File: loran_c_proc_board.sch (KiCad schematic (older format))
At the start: 28 parts, among them P101 Power, P102 Cortex SWD, P103 Clock board, U101 LD1117S33, U102 74AC14, U103 74AC14

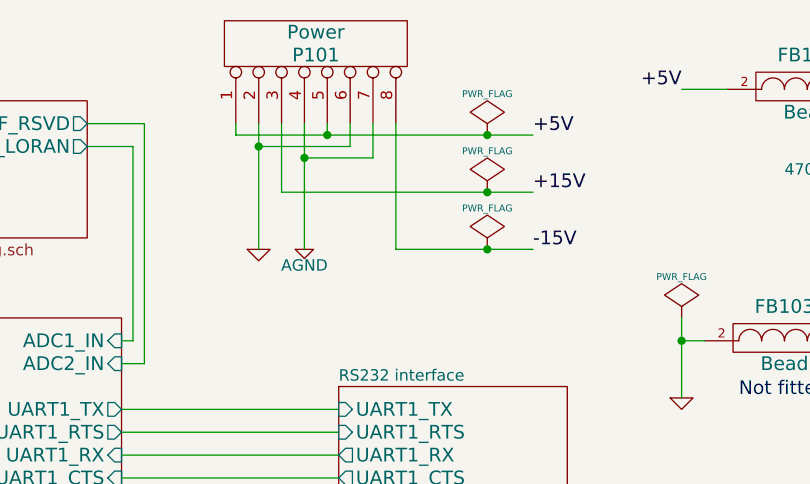
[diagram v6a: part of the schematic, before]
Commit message: Intermediate update: PCB routing/schematic tweaking in process..
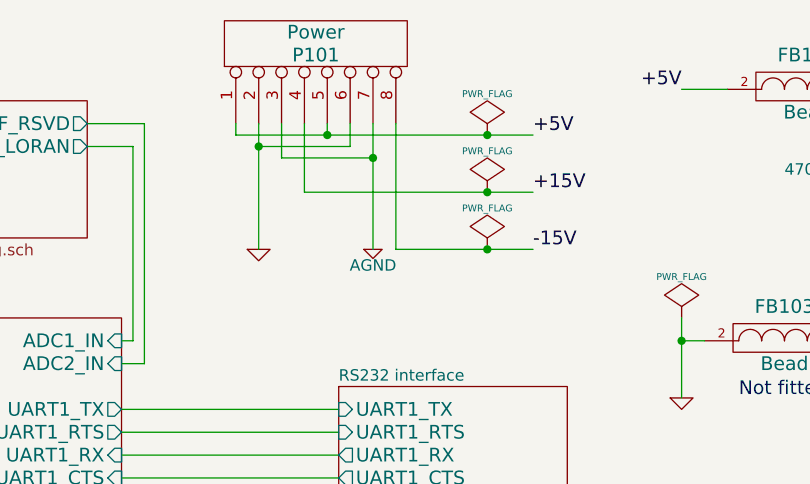
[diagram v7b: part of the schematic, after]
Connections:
- net +15V: now also P101.4 (P4); no longer P101.3 (P3)
- net AGND: now also P101.3 (P3); no longer P101.4 (P4)
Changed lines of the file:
@@
 L AGND #PWR012
 U 1 1 52E69A33
-P 5000 1850
-F 0 "#PWR012" H 5000 1850 40  0001 C CNN
-F 1 "AGND" H 5000 1780 50  0000 C CNN
-F 2 "" H 5000 1850 60  0000 C CNN
-F 3 "" H 5000 1850 60  0000 C CNN
-	1    5000 1850
+P 5300 1850
+F 0 "#PWR012" H 5300 1850 40  0001 C CNN
+F 1 "AGND" H 5300 1780 50  0000 C CNN
+F 2 "" H 5300 1850 60  0000 C CNN
+F 3 "" H 5300 1850 60  0000 C CNN
+	1    5300 1850
 	1    0    0    -1
 $EndComp
@@
 	5200 1400 5200 1300
 Wire Wire Line
-	5000 1300 5000 1850
-Wire Wire Line
-	5000 1450 5300 1450
-Wire Wire Line
-	5300 1450 5300 1300
+	4900 1450 5300 1450
+Wire Wire Line
+	5300 1300 5300 1850
 Connection ~ 5100 1350
 Wire Wire Line
-	4900 1300 4900 1600
-Wire Wire Line
-	4900 1600 6000 1600
+	5000 1600 6000 1600
 Wire Wire Line
 	5400 1300 5400 1850
@@
 Connection ~ 5800 1850
 Connection ~ 4800 1400
-Connection ~ 5000 1450
+Wire Wire Line
+	5000 1300 5000 1600
+Wire Wire Line
+	4900 1300 4900 1450
+Connection ~ 5300 1450
 $EndSCHEMATC

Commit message: Intermediate update #2: PCB routing/schematic tweaking in process
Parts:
- added MH101, MH102, MH103, MH104: HOLE, symbol HOLE
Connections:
- net GNDPWR: now also MH103.1, MH104.1
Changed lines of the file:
@@
 LIBS:transf
 LIBS:video
+LIBS:led_holder
 LIBS:loran_c_proc_board-cache
 EELAYER 24 0
@@
 	4900 1300 4900 1450
 Connection ~ 5300 1450
+$Comp
+L HOLE MH104
+U 1 1 52EF52BD
+P 1800 1800
+F 0 "MH104" H 1800 2000 60  0000 C CNN
+F 1 "HOLE" H 1800 1620 60  0000 C CNN
+F 2 "" H 1800 1800 60  0000 C CNN
+F 3 "" H 1800 1800 60  0000 C CNN
+	1    1800 1800
+	1    0    0    -1
+$EndComp
+$Comp
+L HOLE MH103
+U 1 1 52EF53B0
+P 1800 1250
+F 0 "MH103" H 1800 1450 60  0000 C CNN
+F 1 "HOLE" H 1800 1070 60  0000 C CNN
+F 2 "" H 1800 1250 60  0000 C CNN
+F 3 "" H 1800 1250 60  0000 C CNN
+	1    1800 1250
+	1    0    0    -1
+$EndComp
+$Comp
+L HOLE MH101
+U 1 1 52EF7090
+P 1000 1250
+F 0 "MH101" H 1000 1450 60  0000 C CNN
+F 1 "HOLE" H 1000 1070 60  0000 C CNN
+F 2 "" H 1000 1250 60  0000 C CNN
+F 3 "" H 1000 1250 60  0000 C CNN
+	1    1000 1250
+	1    0    0    -1
+$EndComp
+$Comp
+L HOLE MH102
+U 1 1 52EF741F
+P 1000 1800
+F 0 "MH102" H 1000 2000 60  0000 C CNN
+F 1 "HOLE" H 1000 1620 60  0000 C CNN
+F 2 "" H 1000 1800 60  0000 C CNN
+F 3 "" H 1000 1800 60  0000 C CNN
+	1    1000 1800
+	1    0    0    -1
+$EndComp
+$Comp
+L GNDPWR #PWR037
+U 1 1 52EF788F
+P 1400 2100
+F 0 "#PWR037" H 1400 2150 40  0001 C CNN
+F 1 "GNDPWR" H 1400 2020 40  0000 C CNN
+F 2 "" H 1400 2100 60  0000 C CNN
+F 3 "" H 1400 2100 60  0000 C CNN
+	1    1400 2100
+	1    0    0    -1
+$EndComp
+Wire Wire Line
+	1600 1800 1400 1800
+Wire Wire Line
+	1400 1250 1400 2100
+Wire Wire Line
+	1600 1250 1400 1250
+Connection ~ 1400 1800
 $EndSCHEMATC
